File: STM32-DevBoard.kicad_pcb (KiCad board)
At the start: 2 copper layers, 55 parts, among them J1 I2C Bus 1, J2 Serial Debugger, J3 USART1, J4 12402012E212A, J5 PJ-002A, Q1 AO3401A, SW1 SW_SPDT, U1 STM32F103C8T6, U2 TPS563209DDCR, U3 USBLC6-2SC6, Y1 16MHz

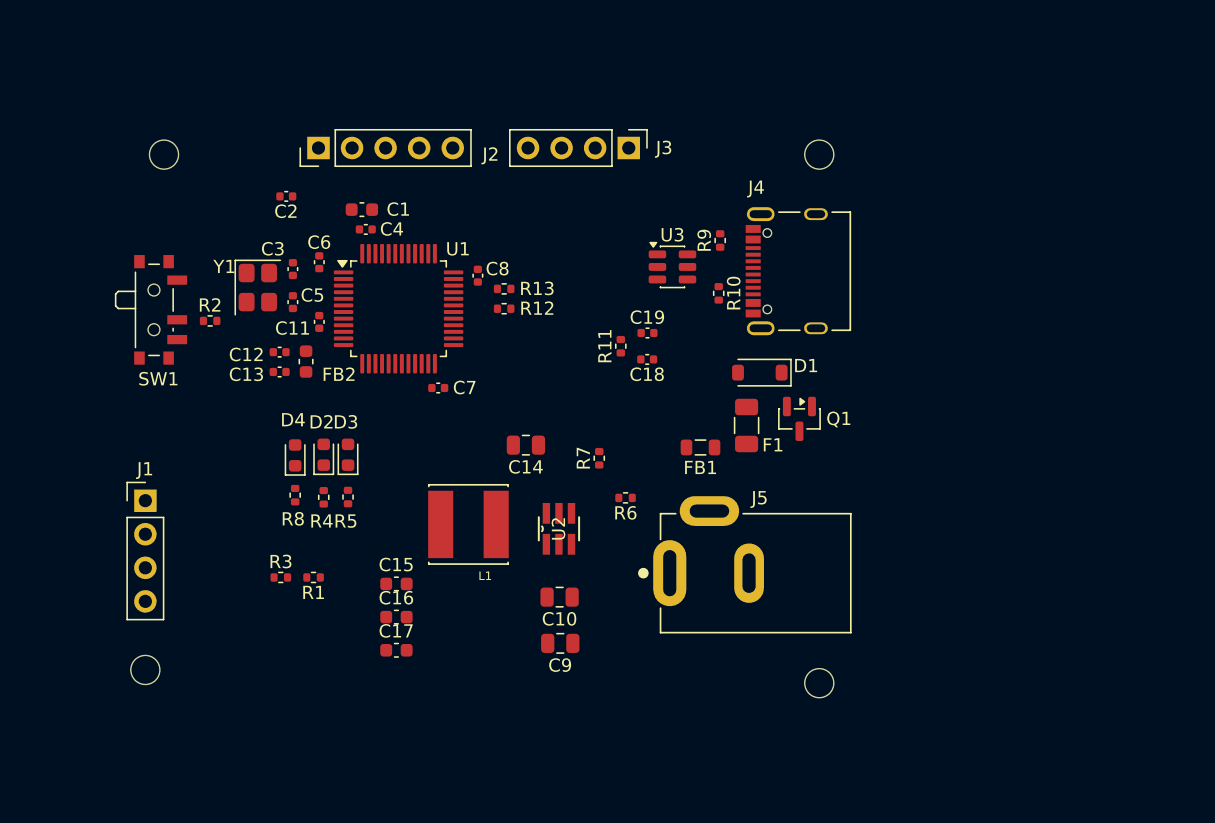
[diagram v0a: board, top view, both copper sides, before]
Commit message: Board constraints, layout, and initial traces done
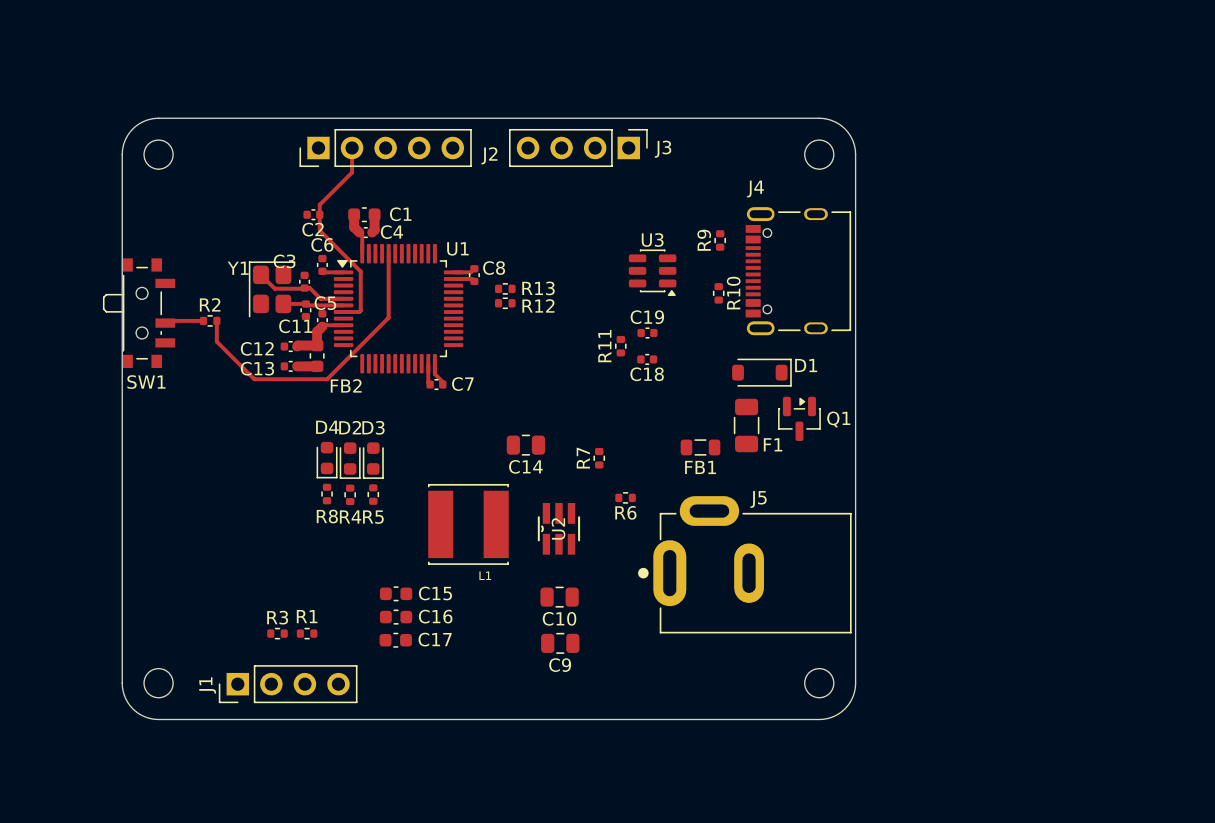
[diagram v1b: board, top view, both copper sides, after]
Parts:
- moved J1 15.5 mm to (123.5, 127.6), turned to 90 degrees
- moved R1 4.28 mm to (128.7, 123.8)
- moved R3 4.26 mm to (126.5, 123.8)
- moved C2 2.48 mm to (129.2, 92.0)
- moved D4 2.42 mm to (130.2, 110.5)
- moved R8 2.41 mm to (130.2, 113.2)
- moved D2 2.02 mm to (132.0, 110.5)
- moved R4 2.01 mm to (132.0, 113.2)
- moved D3 1.93 mm to (133.8, 110.5)
- moved R5 1.92 mm to (133.8, 113.2)
- moved U3 1.53 mm to (154.9, 96.3), turned to 180 degrees
- moved H3 1.41 mm to (117.5, 127.5)
- moved C3 1.31 mm to (128.6, 97.1)
- moved C5 1.16 mm to (128.7, 99.3)
- moved Y1 1.10 mm to (126.1, 97.7)
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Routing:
- net /BOOT0: track 0.00 -> 22.5 mm
- net NRST: track 0.00 -> 15.9 mm
- net +3.3V: track 0.00 -> 9.87 mm
- net /HSE_IN: track 0.00 -> 7.04 mm
- net +3.3VA: track 0.00 -> 4.80 mm
- net GND: track 0.00 -> 4.71 mm
- net /HSE_OUT: track 0.00 -> 4.60 mm
- net /SW_BOOT0: track 0.00 -> 2.95 mm
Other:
- board outline added: 55.5 x 45.5 mm
- copper layers 2 -> 4

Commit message: Added footprints and models, progressed PCB layout. TODO: rename nets
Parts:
- removed the R12 at (143.7, 98.8)
- removed the R13 at (143.7, 97.7)
- removed the R8 at (130.2, 113.2)
- added J1: Conn_01x08_Pin, Connector_PinHeader_1.00mm:PinHeader_1x08_P1.00mm_Vertical, F.Cu at (116.9, 110.5)
- added R11: 1K, Resistor_SMD:R_0402_1005Metric, F.Cu at (192.0, 93.5)
- added R6: 1K, Resistor_SMD:R_0402_1005Metric, F.Cu at (191.2, 102.9)
- added R9: 10k, Resistor_SMD:R_0402_1005Metric, F.Cu at (192.0, 91.5)
- C1: footprint Capacitor_SMD:C_0603_1608Metric -> Capacitor_SMD:C_0805_2012Metric
- C10: value 10uF -> 100n; footprint Capacitor_SMD:C_0805_2012Metric -> Capacitor_SMD:C_0402_1005Metric
- C11: value 10n -> 10u; footprint Capacitor_SMD:C_0402_1005Metric -> Capacitor_SMD:C_0805_2012Metric
- C14: value 100nF -> 100n; footprint Capacitor_SMD:C_0805_2012Metric -> Capacitor_SMD:C_0402_1005Metric
- C9: value 10uF -> 10u
- D4: value RED -> LED1
- J3: renamed from J2; value Serial Debugger -> Serial Debug
- L1: value VLS6045EX-2R2N -> 2.2u
- R4, R5: value 1K -> 22R
- R7: value 10k -> 1K
- moved R4 64.5 mm to (192.0, 89.5), turned to 0 degrees
- moved R5 60.3 mm to (193.2, 102.9), turned to -90 degrees
- moved C11 28.5 mm to (147.9, 122.1), turned to 180 degrees
- moved C10 27.6 mm to (129.8, 100.1), turned to 90 degrees
- moved C6 11.7 mm to (141.6, 96.6), turned to -90 degrees
- moved C8 11.5 mm to (129.9, 95.8), turned to 90 degrees
- moved D4 7.76 mm to (133.9, 117.3), turned to 0 degrees
- moved C2 2.85 mm to (130.3, 89.4)
- moved C14 0.97 mm to (146.1, 110.0), turned to 0 degrees
- moved L1 0.72 mm to (141.6, 115.8)
- moved FB2 0.72 mm to (129.4, 103.5)
- moved C12 0.68 mm to (127.4, 102.7)
- moved C13 0.68 mm to (127.4, 104.2)
- moved C1 0.25 mm to (133.1, 91.8)
- moved C7 0.11 mm to (138.6, 105.0)
- renumbered J1 to J2, J3 to J4, J4 to J5, J5 to J6, R9 to R10, R10 to R12, R11 to R13, R6 to R8
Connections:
- C10 pad 1: /VIN -> +3.3VA
- C11 pad 1: +3.3VA -> /VIN
- C14 pad 1: Net-(U2-VBST) -> Net-(U2-SW)
- C14 pad 2: Net-(U2-SW) -> Net-(U2-VBST)
- C19 pad 1: Net-(C19-Pad1) -> VBUSF
- D1 pad 2: VBUS -> VBUSF
- R13 pad 2: Net-(C19-Pad1) -> VBUSF
- R4 pad 1: Net-(D2-K) -> Net-(U1-PA11)
- R4 pad 2: GND -> USB_D-
- R5 pad 1: Net-(D3-K) -> Net-(U1-PA12)
- R5 pad 2: GND -> USB_D+
- R7 pad 1: Net-(U2-VFB) -> Net-(D3-K)
- U1 pad 10: unconnected-(U1-PA0-Pad10) -> GPIO6
- U1 pad 11: unconnected-(U1-PA1-Pad11) -> Net-(D2-A)
- U1 pad 12: unconnected-(U1-PA2-Pad12) -> Net-(D3-A)
- U1 pad 13: Net-(D2-A) -> GPIO1
- U1 pad 14: Net-(D3-A) -> GPIO2
- U1 pad 15: unconnected-(U1-PA5-Pad15) -> GPIO3
- U1 pad 16: unconnected-(U1-PA6-Pad16) -> GPIO4
- U1 pad 17: unconnected-(U1-PA7-Pad17) -> GPIO5
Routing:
- net /BOOT0: track 22.5 -> 0.00 mm
- net NRST: track 15.9 -> 0.00 mm
- net +3.3VA: track 4.80 -> 0.00 mm
- net +3.3V: track 9.87 -> 5.14 mm
- net GND: track 4.71 -> 3.28 mm

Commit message: Completed net names
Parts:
- J3: value Serial Debug -> Serial Debugger
- moved R6 59.6 mm to (131.8, 107.6)
- moved R5 45.2 mm to (148.4, 96.5), turned to 0 degrees
- moved R4 44.3 mm to (148.4, 97.6)
- moved U3 1.37 mm to (153.5, 96.5)
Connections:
- net Net-(D1-K) renamed /VIN_PROTECTED
- net Net-(D2-A) renamed /LED1
- net Net-(D3-A) renamed /LED2
- net Net-(F1-Pad2) renamed /VIN_FUSED
- net Net-(J5-CC1_A) renamed /CC1_A
- net Net-(J5-CC1_B) renamed /CC1_B
- net Net-(J5-D+_A) renamed /DP_AB
- net Net-(J5-D-_A) renamed /DN_AB
- net Net-(U1-PA11) renamed /USB_DN
- net Net-(U1-PA12) renamed /USB_DP
- net Net-(U2-SW) renamed /SW_OUT
- net Net-(U2-VBST) renamed /VBST_OUT
- net Net-(U2-VFB) renamed /VFB_OUT

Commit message: Routing progressed
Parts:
- D4: value LED1 -> PLED
- J1: footprint Connector_PinHeader_1.00mm:PinHeader_1x08_P1.00mm_Vertical -> Connector_PinHeader_2.00mm:PinHeader_1x08_P2.00mm_Vertical
- moved R11 75.0 mm to (118.1, 106.6)
- moved R9 45.1 mm to (151.3, 111.0), turned to 90 degrees
- moved R7 33.5 mm to (118.1, 103.1), turned to 180 degrees
- moved D4 17.0 mm to (120.7, 106.6)
- moved C2 15.1 mm to (145.4, 88.9)
- moved D3 15.0 mm to (120.7, 103.1), turned to 0 degrees
- moved R4 14.1 mm to (158.7, 88.0)
- moved J4 14.1 mm to (139.0, 86.6)
- moved R6 13.9 mm to (118.1, 104.8), turned to 180 degrees
- moved J3 13.9 mm to (143.5, 86.6)
- moved D2 12.6 mm to (120.7, 104.8), turned to 0 degrees
- moved R2 3.59 mm to (121.4, 96.5)
- moved SW1 3.59 mm to (116.5, 95.9)
- moved C19 3.00 mm to (154.5, 104.0)
- moved C15 2.16 mm to (137.3, 121.9)
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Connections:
- net /LED1 renamed /LED1+
- net /LED2 renamed /LED2+
- net Net-(D2-K) renamed /LED1-
- net Net-(D3-K) renamed /LED2-
- net Net-(D4-K) renamed /PLED_OUT
- J5 pad A6: /DP_AB -> USB_D+
- J5 pad A7: /DN_AB -> USB_D-
- J5 pad B6: /DP_AB -> USB_D+
- J5 pad B7: /DN_AB -> USB_D-
- R4 pad 1: /USB_DN -> unconnected-(R4-Pad1)
- R4 pad 2: USB_D- -> unconnected-(R4-Pad2)
- R5 pad 1: /USB_DP -> unconnected-(R5-Pad1)
- R5 pad 2: USB_D+ -> unconnected-(R5-Pad2)
- U1 pad 32: /USB_DN -> USB_D-
- U1 pad 33: /USB_DP -> USB_D+
- U3 pad 1: /DP_AB -> USB_D+
- U3 pad 3: /DN_AB -> USB_D-
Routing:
- net I2C1_SDA: track 0.00 -> 28.8 mm
- net I2C1_SCL: track 0.00 -> 27.9 mm
- net USB_D+: track 0.00 -> 24.7 mm
- net USB_D-: track 0.00 -> 22.0 mm
- net SWDIO: track 0.00 -> 18.7 mm
- net GPIO5: track 0.00 -> 18.4 mm
- net VBUS: track 0.00 -> 16.8 mm
- net GPIO4: track 0.00 -> 16.0 mm
- net /LED1+: track 0.00 -> 15.4 mm
- net GPIO3: track 0.00 -> 14.3 mm
- net SWCLK: track 0.00 -> 14.0 mm
- net /LED2+: track 0.00 -> 13.6 mm
- net VBUSF: track 0.00 -> 9.53 mm
- net USART1_RX: track 0.00 -> 9.01 mm
- net USART1_TX: track 0.00 -> 8.63 mm
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
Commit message: Routing Complete, need to finish off net labels
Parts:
- moved R4 12.1 mm to (150.5, 96.9)
- moved C15 3.43 mm to (136.6, 118.5)
- moved C16 3.43 mm to (136.6, 120.3)
- moved C17 3.43 mm to (136.6, 122.0)
- moved C9 2.70 mm to (148.4, 121.8)
- moved L1 2.61 mm to (141.1, 113.1)
- moved R8 2.61 mm to (153.7, 110.3)
- moved U2 2.61 mm to (148.3, 113.3)
- moved R9 2.61 mm to (151.8, 108.4)
- moved C11 2.61 mm to (148.4, 119.5)
- moved FB2 2.39 mm to (127.7, 101.1), turned to 180 degrees
- moved C12 1.41 mm to (128.7, 102.9), turned to -90 degrees
- moved C14 1.10 mm to (145.8, 108.9)
- moved R5 1.05 mm to (150.5, 95.9)
- moved R3 1.00 mm to (125.5, 123.8), turned to 180 degrees
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- renumbered D2 to LED1, D3 to LED2, D4 to PLED
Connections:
- net /VIN renamed /+VIN_FILTERED
- net /VIN_FUSED renamed /+VIN_FUSED
- net /VIN_PROTECTED renamed /+VIN_PROTECTED
- J5 pad A6: USB_D+ -> /USBC_D+
- J5 pad A7: USB_D- -> /USBC_D-
- J5 pad B6: USB_D+ -> /USBC_D+
- J5 pad B7: USB_D- -> /USBC_D-
- R4 pad 1: unconnected-(R4-Pad1) -> Net-(U1-PA11)
- R4 pad 2: unconnected-(R4-Pad2) -> USB_D-
- R5 pad 1: unconnected-(R5-Pad1) -> Net-(U1-PA12)
- R5 pad 2: unconnected-(R5-Pad2) -> USB_D+
- U1 pad 10: GPIO6 -> unconnected-(U1-PA0-Pad10)
- U1 pad 18: unconnected-(U1-PB0-Pad18) -> GPIO6
- U1 pad 32: USB_D- -> Net-(U1-PA11)
- U1 pad 33: USB_D+ -> Net-(U1-PA12)
- U3 pad 1: USB_D+ -> /USBC_D+
- U3 pad 3: USB_D- -> /USBC_D-
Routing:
- net +3.3V: track 10.1 -> 157.4 mm, vias 0 -> 8
- net GND: track 10.1 -> 57.7 mm, vias 0 -> 66
- net GPIO6: track 0.00 -> 29.2 mm
- net /BOOT0: track 0.00 -> 22.6 mm
- net USB_D+: track 24.7 -> 3.42 mm
- net GPIO1: track 0.00 -> 21.1 mm
- net USB_D-: track 22.0 -> 3.38 mm
- net /+VIN_FILTERED: track 0.00 -> 18.1 mm, vias 0 -> 2
- net GPIO2: track 6.94 -> 22.7 mm
- net NRST: track 7.16 -> 22.4 mm, vias 0 -> 2
- net Net-(U1-PA12): track 0.00 -> 11.0 mm
- net Net-(U1-PA11): track 0.00 -> 11.0 mm
- net VBUS: track 16.8 -> 27.2 mm
- net GPIO3: track 14.3 -> 24.4 mm
- net GPIO4: track 16.0 -> 26.0 mm
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- added copper zone on F.Cu, net +12V
- added copper zone on F.Cu, net +3.3V
- added copper zone on F.Cu, net /+VIN_FILTERED
- added copper zone on B.Cu, net /SW_OUT
- added copper zone on F.Cu, net /SW_OUT
- added copper zone on B.Cu, net GND
- added copper zone on F.Cu, net GND
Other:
- copper layers 4 -> 2
